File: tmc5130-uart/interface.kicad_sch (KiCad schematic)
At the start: 12 parts, among them J301 FFC_P1mm_BOT_RA_SMD, M301 Fan_5VDC_25x25x8mm, U301 TPSM365R6V5RDNR

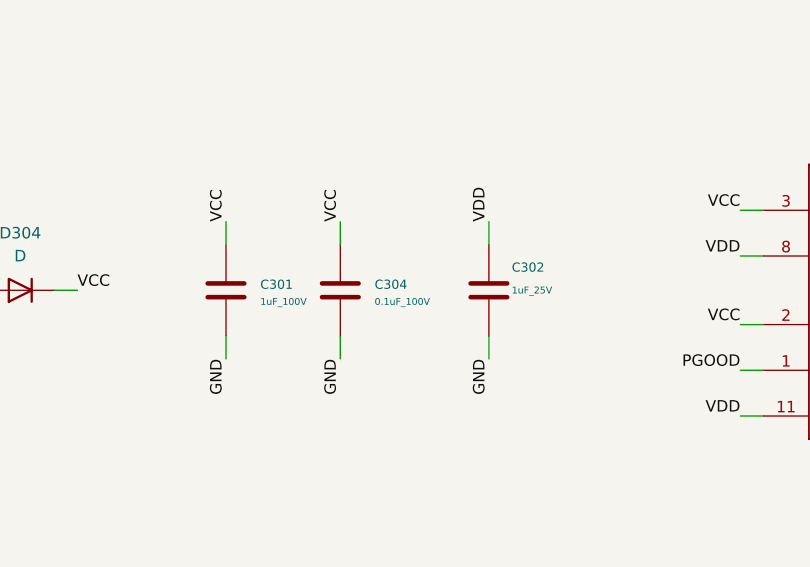
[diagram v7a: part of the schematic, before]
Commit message: Change capacitor
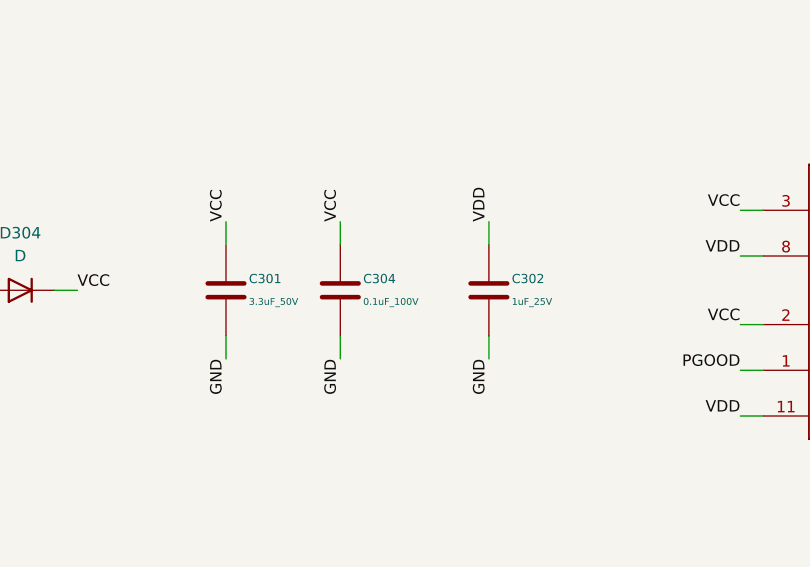
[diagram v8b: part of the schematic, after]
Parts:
- removed C301: 1uF_100V, Janelia:C_1206_3216Metric, symbol Janelia:C_1uF_100V_1206
- added C301: 3.3uF_50V, Janelia:C_1210_3225Metric, symbol Janelia:C_3.3uF_50V_1210
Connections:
- net GND: now also C301.2
- net VCC: now also C301.1
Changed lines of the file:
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@@
+    )
+  )
+  (symbol (lib_id "Janelia:C_3.3uF_50V_1210") (at 132.08 68.58 0) (unit 1)
+    (in_bom yes) (on_board yes) (dnp no)
+    (property "Reference" "C301" (at 134.62 67.31 0)
+      (effects (font (size 1.016 1.016)) (justify left))
+    )
+    (property "Value" "3.3uF_50V" (at 134.62 69.85 0)
+      (effects (font (size 0.762 0.762)) (justify left))
+    )
+    (property "Footprint" "Janelia:C_1210_3225Metric" (at 133.0452 72.39 0)
+      (effects (font (size 0.762 0.762)) hide)
+    )
+    (property "Datasheet" "" (at 132.08 68.58 0)
+      (effects (font (size 1.524 1.524)) hide)
+    )
+    (property "Vendor" "JLCPCB" (at 134.62 63.5 0)
+      (effects (font (size 1.524 1.524)) hide)
+    )
+    (property "Vendor Part Number" "C1021610" (at 137.16 60.96 0)
+      (effects (font (size 1.524 1.524)) hide)
+    )
+    (property "Synopsis" "50V 3.3uF" (at 139.7 58.42 0)
+      (effects (font (size 1.524 1.524)) hide)
+    )
+    (property "Package" "1210" (at 132.08 68.58 0)
+      (effects (font (size 1.27 1.27)) hide)
+    )
+    (property "Manufacturer" "PSA(Prosperity Dielectrics)" (at 132.08 68.58 0)
+      (effects (font (size 1.27 1.27)) hide)
+    )
+    (property "Manufacturer Part Number" "FS32X335K500EGG" (at 132.08 68.58 0)
+      (effects (font (size 1.27 1.27)) hide)
+    )
+    (property "LCSC" "C1021610" (at 132.08 68.58 0)
+      (effects (font (size 1.27 1.27)) hide)
+    )
+    (pin "1")
+    (pin "2")
+    (instances
+      (project "tmc5130-uart"
+        (path "/df2b2e89-e055-4140-95de-f1df723db034/c1dd8f61-494c-402f-8e59-08309c64fc3f"
+          (reference "C301") (unit 1)
+        )
+      )
     )
   )
   (symbol (lib_id "Janelia:C_1uF_25V_0402") (at 161.29 68.58 0) (unit 1)
     (in_bom yes) (on_board yes) (dnp no)
-    (property "Reference" "C302" (at 163.83 66.04 0)
-      (effects (font (size 1.016 1.016)) (justify left))
-    )
-    (property "Value" "1uF_25V" (at 163.83 68.58 0)
+    (property "Reference" "C302" (at 163.83 67.31 0)
+      (effects (font (size 1.016 1.016)) (justify left))
+    )
+    (property "Value" "1uF_25V" (at 163.83 69.85 0)
       (effects (font (size 0.762 0.762)) (justify left))
     )
@@
     )
   )
-  (symbol (lib_id "Janelia:C_1uF_100V_1206") (at 132.08 68.58 0) (unit 1)
-    (in_bom yes) (on_board yes) (dnp no) (fields_autoplaced)
-    (property "Reference" "C301" (at 135.89 67.945 0)
-      (effects (font (size 1.016 1.016)) (justify left))
-    )
-    (property "Value" "1uF_100V" (at 135.89 69.8499 0)
-      (effects (font (size 0.762 0.762)) (justify left))
-    )
-    (property "Footprint" "Janelia:C_1206_3216Metric" (at 133.0452 72.39 0)
-      (effects (font (size 0.762 0.762)) hide)
-    )
-    (property "Datasheet" "" (at 132.08 68.58 0)
-      (effects (font (size 1.524 1.524)) hide)
-    )
-    (property "Vendor" "JLCPCB" (at 134.62 63.5 0)
-      (effects (font (size 1.524 1.524)) hide)
-    )
-    (property "Vendor Part Number" "C840122" (at 137.16 60.96 0)
-      (effects (font (size 1.524 1.524)) hide)
-    )
-    (property "Synopsis" "100V 1uF X7R ±20% 1206" (at 139.7 58.42 0)
-      (effects (font (size 1.524 1.524)) hide)
-    )
-    (property "Package" "1206" (at 132.08 68.58 0)
-      (effects (font (size 1.27 1.27)) hide)
-    )
-    (property "Manufacturer" "HUI JU" (at 132.08 68.58 0)
-      (effects (font (size 1.27 1.27)) hide)
-    )
-    (property "Manufacturer Part Number" "NC1206B105M101CEPN" (at 132.08 68.58 0)
-      (effects (font (size 1.27 1.27)) hide)
-    )
-    (property "LCSC" "C840122" (at 132.08 68.58 0)
-      (effects (font (size 1.27 1.27)) hide)
-    )
-    (pin "1")
-    (pin "2")
-    (instances
-      (project "tmc5130-uart"
-        (path "/df2b2e89-e055-4140-95de-f1df723db034/c1dd8f61-494c-402f-8e59-08309c64fc3f"
-          (reference "C301") (unit 1)
-        )
-      )
-    )
-  )
   (symbol (lib_id "Janelia:C_0.1uF_100V_0402") (at 144.78 68.58 0) (unit 1)
-    (in_bom yes) (on_board yes) (dnp no) (fields_autoplaced)
-    (property "Reference" "C304" (at 148.59 67.945 0)
-      (effects (font (size 1.016 1.016)) (justify left))
-    )
-    (property "Value" "0.1uF_100V" (at 148.59 69.8499 0)
-      (effects (font (size 0.762 0.762)) (justify left))
-    )
+    (in_bom yes) (on_board yes) (dnp no)
+    (property "Reference" "C304" (at 147.32 67.31 0)
+      (effects (font (size 1.016 1.016)) (justify left))
+    )
+    (property "Value" "0.1uF_100V" (at 147.32 69.85 0)
+      (effects (font (size 0.762 0.762)) (justify left))
+    )
